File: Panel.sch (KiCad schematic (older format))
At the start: 11 parts, among them J7 Rotated_Barrel, U7 LM3406HV

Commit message: Removed the LV-Caps with the HV-Caps to remain consistent
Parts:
- C24, C26: footprint Capacitor_SMD:C_0603_1608Metric -> Capacitor_SMD:C_0805_2012Metric; Buy https://www.digikey.com/product-detail/en/murata-electronics-north-america/GCM188R71C104KA37D/490-4774-1-ND/1641693 -> https://www.digikey.com/product-detail/en/murata-electronics-north-america/GCM21BR72A104KA37L/490-4789-1-ND/1641708
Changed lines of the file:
@@
 F 0 "C29" H 1785 2220 50  0000 L CNN
 F 1 "100nF" H 1785 2070 50  0000 L CNN
-F 2 "Capacitor_SMD:C_0603_1608Metric" H 1775 2150 50  0001 C CNN
+F 2 "Capacitor_SMD:C_0805_2012Metric" H 1775 2150 50  0001 C CNN
 F 3 "" H 1775 2150 50  0001 C CNN
-F 4 "https://www.digikey.com/product-detail/en/murata-electronics-north-america/GCM188R71C104KA37D/490-4774-1-ND/1641693" H 1775 2150 60  0001 C CNN "Buy"
+F 4 "https://www.digikey.com/product-detail/en/murata-electronics-north-america/GCM21BR72A104KA37L/490-4789-1-ND/1641708" H 1775 2150 60  0001 C CNN "Buy"
 	1    1775 2150
 	1    0    0    -1
@@
 F 0 "C31" H 2985 2220 50  0000 L CNN
 F 1 "100nF" H 2985 2070 50  0000 L CNN
-F 2 "Capacitor_SMD:C_0603_1608Metric" H 2975 2150 50  0001 C CNN
+F 2 "Capacitor_SMD:C_0805_2012Metric" H 2975 2150 50  0001 C CNN
 F 3 "" H 2975 2150 50  0001 C CNN
-F 4 "https://www.digikey.com/product-detail/en/murata-electronics-north-america/GCM188R71C104KA37D/490-4774-1-ND/1641693" H 2975 2150 50  0001 C CNN "Buy"
+F 4 "https://www.digikey.com/product-detail/en/murata-electronics-north-america/GCM21BR72A104KA37L/490-4789-1-ND/1641708" H 2975 2150 50  0001 C CNN "Buy"
 	1    2975 2150
 	1    0    0    -1

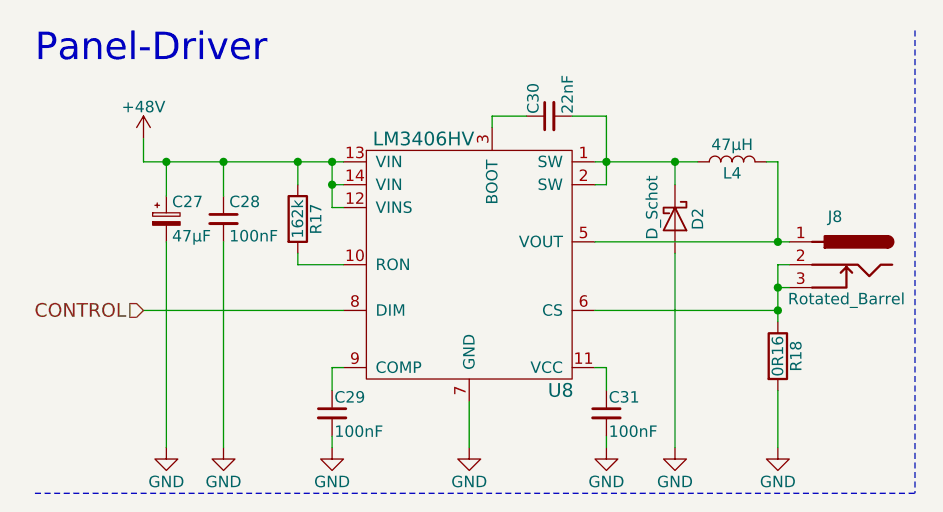
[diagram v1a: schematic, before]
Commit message: Replaced the 160mOhms-Resistor with an in-stock-one
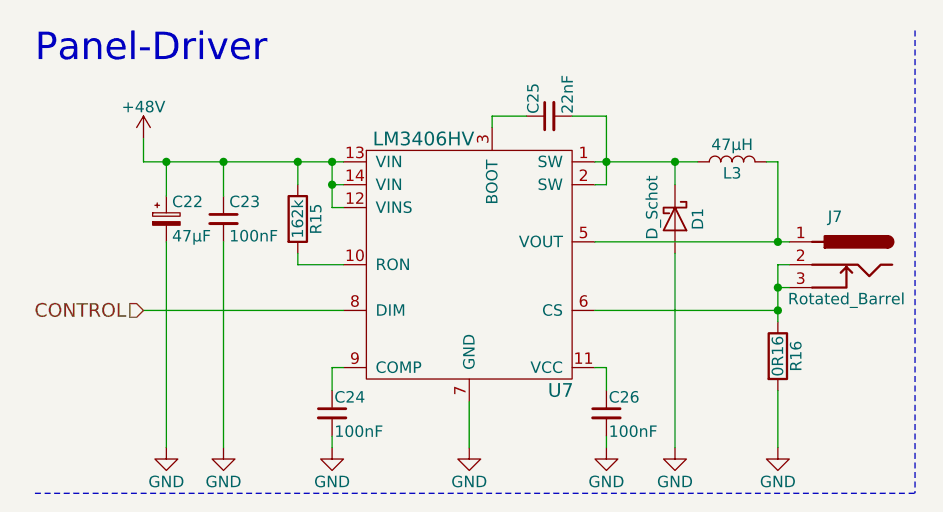
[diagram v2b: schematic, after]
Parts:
- R16: footprint Resistor_SMD:R_0805_2012Metric -> Resistor_SMD:R_1206_3216Metric; Buy https://www.digikey.com/product-detail/en/panasonic-electro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 -> https://www.digikey.com/product-detail/en/te-connectivity-p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
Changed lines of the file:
@@
 $Descr A4 11693 8268
 encoding utf-8
-Sheet 4 7
+Sheet 3 7
 Title ""
 Date "2018-02-14"
@@
 AR Path="/5A4C34AF/5A7753B7" Ref="R15"  Part="1"
 AR Path="/5A4C3F5F/5A7753B7" Ref="R17"  Part="1"
-F 0 "R17" V 1705 1300 50  0000 C CNN
+F 0 "R15" V 1705 1300 50  0000 C CNN
 F 1 "162k" V 1625 1300 50  0000 C CNN
 F 2 "Resistor_SMD:R_0603_1608Metric" V 1555 1300 50  0001 C CNN
@@
 AR Path="/5A4C34AF/5A77745B" Ref="C24"  Part="1"
 AR Path="/5A4C3F5F/5A77745B" Ref="C29"  Part="1"
-F 0 "C29" H 1785 2220 50  0000 L CNN
+F 0 "C24" H 1785 2220 50  0000 L CNN
 F 1 "100nF" H 1785 2070 50  0000 L CNN
 F 2 "Capacitor_SMD:C_0805_2012Metric" H 1775 2150 50  0001 C CNN
@@
 AR Path="/5A4C34AF/5A777BDD" Ref="#PWR063"  Part="1"
 AR Path="/5A4C3F5F/5A777BDD" Ref="#PWR071"  Part="1"
-F 0 "#PWR071" H 1775 2050 50  0001 C CNN
+F 0 "#PWR063" H 1775 2050 50  0001 C CNN
 F 1 "GND" H 1775 2150 50  0000 C CNN
 F 2 "" H 1775 2300 50  0001 C CNN
@@
 AR Path="/5A4C34AF/5A777CD4" Ref="C26"  Part="1"
 AR Path="/5A4C3F5F/5A777CD4" Ref="C31"  Part="1"
-F 0 "C31" H 2985 2220 50  0000 L CNN
+F 0 "C26" H 2985 2220 50  0000 L CNN
 F 1 "100nF" H 2985 2070 50  0000 L CNN
 F 2 "Capacitor_SMD:C_0805_2012Metric" H 2975 2150 50  0001 C CNN
@@
 AR Path="/5A4C34AF/5A777CDA" Ref="#PWR065"  Part="1"
 AR Path="/5A4C3F5F/5A777CDA" Ref="#PWR073"  Part="1"
-F 0 "#PWR073" H 2975 2050 50  0001 C CNN
+F 0 "#PWR065" H 2975 2050 50  0001 C CNN
 F 1 "GND" H 2975 2150 50  0000 C CNN
 F 2 "" H 2975 2300 50  0001 C CNN
@@
 AR Path="/5A4C34AF/5A777FA3" Ref="#PWR064"  Part="1"
 AR Path="/5A4C3F5F/5A777FA3" Ref="#PWR072"  Part="1"
-F 0 "#PWR072" H 2375 2050 50  0001 C CNN
+F 0 "#PWR064" H 2375 2050 50  0001 C CNN
 F 1 "GND" H 2375 2150 50  0000 C CNN
 F 2 "" H 2375 2300 50  0001 C CNN
@@
 AR Path="/5A4C34AF/5A77816D" Ref="C25"  Part="1"
 AR Path="/5A4C3F5F/5A77816D" Ref="C30"  Part="1"
-F 0 "C30" H 2735 920 50  0000 L CNN
+F 0 "C25" H 2735 920 50  0000 L CNN
 F 1 "22nF" H 2735 770 50  0000 L CNN
 F 2 "Capacitor_SMD:C_0603_1608Metric" H 2725 850 50  0001 C CNN
@@
 AR Path="/5A4C34AF/5A77899A" Ref="L3"  Part="1"
 AR Path="/5A4C3F5F/5A77899A" Ref="L4"  Part="1"
-F 0 "L4" V 3475 1050 50  0000 C CNN
+F 0 "L3" V 3475 1050 50  0000 C CNN
 F 1 "47μH" V 3600 1050 50  0000 C CNN
 F 2 "" H 3525 1050 50  0001 C CNN
@@
 AR Path="/5A4C34AF/5A7789F9" Ref="D1"  Part="1"
 AR Path="/5A4C3F5F/5A7789F9" Ref="D2"  Part="1"
-F 0 "D2" H 3275 1400 50  0000 C CNN
+F 0 "D1" H 3275 1400 50  0000 C CNN
 F 1 "D_Schot" H 3225 1200 50  0000 C CNN
 F 2 "Diode_SMD:D_SMA_Handsoldering" H 3275 1300 50  0001 C CNN
@@
 AR Path="/5A4C34AF/5A778B62" Ref="#PWR066"  Part="1"
 AR Path="/5A4C3F5F/5A778B62" Ref="#PWR074"  Part="1"
-F 0 "#PWR074" H 3275 2050 50  0001 C CNN
+F 0 "#PWR066" H 3275 2050 50  0001 C CNN
 F 1 "GND" H 3275 2150 50  0000 C CNN
 F 2 "" H 3275 2300 50  0001 C CNN
@@
 AR Path="/5A4C34AF/5A779AD3" Ref="J7"  Part="1"
 AR Path="/5A4C3F5F/5A779AD3" Ref="J8"  Part="1"
-F 0 "J8" H 3975 1710 50  0000 C CNN
+F 0 "J7" H 3975 1710 50  0000 C CNN
 F 1 "Rotated_Barrel" H 4025 1350 50  0000 C CNN
 F 2 "" H 4025 1440 50  0001 C CNN
@@
 AR Path="/5A4C34AF/5A77A2E1" Ref="R16"  Part="1"
 AR Path="/5A4C3F5F/5A77A2E1" Ref="R18"  Part="1"
-F 0 "R18" V 3805 1900 50  0000 C CNN
+F 0 "R16" V 3805 1900 50  0000 C CNN
 F 1 "0R16" V 3725 1900 50  0000 C CNN
-F 2 "Resistor_SMD:R_0805_2012Metric" V 3655 1900 50  0001 C CNN
+F 2 "Resistor_SMD:R_1206_3216Metric" V 3655 1900 50  0001 C CNN
 F 3 "" H 3725 1900 50  0001 C CNN
-F 4 "https://www.digikey.com/product-detail/en/panasonic-electronic-components/ERJ-6DSFR16V/P19313CT-ND/6004668" V 3725 1900 60  0001 C CNN "Buy"
+F 4 "https://www.digikey.com/product-detail/en/te-connectivity-passive-product/RLP73K2BR16FTDF/A109650CT-ND/4032416" V 3725 1900 60  0001 C CNN "Buy"
 	1    3725 1900
 	1    0    0    -1
@@
 AR Path="/5A4C34AF/5A77A9CB" Ref="#PWR067"  Part="1"
 AR Path="/5A4C3F5F/5A77A9CB" Ref="#PWR075"  Part="1"
-F 0 "#PWR075" H 3725 2050 50  0001 C CNN
+F 0 "#PWR067" H 3725 2050 50  0001 C CNN
 F 1 "GND" H 3725 2150 50  0000 C CNN
 F 2 "" H 3725 2300 50  0001 C CNN
@@
 AR Path="/5A4C34AF/5A77D43C" Ref="#PWR062"  Part="1"
 AR Path="/5A4C3F5F/5A77D43C" Ref="#PWR070"  Part="1"
-F 0 "#PWR070" H 1300 2050 50  0001 C CNN
+F 0 "#PWR062" H 1300 2050 50  0001 C CNN
 F 1 "GND" H 1300 2150 50  0000 C CNN
 F 2 "" H 1300 2300 50  0001 C CNN
@@
 AR Path="/5A4C34AF/5A77E620" Ref="U7"  Part="1"
 AR Path="/5A4C3F5F/5A77E620" Ref="U8"  Part="1"
-F 0 "U8" H 2775 950 60  0000 C CNN
+F 0 "U7" H 2775 950 60  0000 C CNN
 F 1 "LM3406HV" H 2175 2050 60  0000 C CNN
 F 2 "Package_SO:TSSOP-14_4.4x5mm_P0.65mm" H 2375 2100 60  0001 C CNN
@@
 AR Path="/5A4C34AF/5A84C99A" Ref="#PWR060"  Part="1"
 AR Path="/5A4C3F5F/5A84C99A" Ref="#PWR068"  Part="1"
-F 0 "#PWR068" H 950 800 50  0001 C CNN
+F 0 "#PWR060" H 950 800 50  0001 C CNN
 F 1 "+48V" H 950 1090 50  0000 C CNN
 F 2 "" H 950 950 50  0001 C CNN
@@
 AR Path="/5A4C34AF/5ABA3DDA" Ref="C22"  Part="1"
 AR Path="/5A4C3F5F/5ABA3DDA" Ref="C27"  Part="1"
-F 0 "C27" H 1075 1375 50  0000 L CNN
+F 0 "C22" H 1075 1375 50  0000 L CNN
 F 1 "47μF" H 1075 1225 50  0000 L CNN
 F 2 "" H 1050 1300 50  0001 C CNN
@@
 AR Path="/5A4C34AF/5ABA5E6C" Ref="C23"  Part="1"
 AR Path="/5A4C3F5F/5ABA5E6C" Ref="C28"  Part="1"
-F 0 "C28" H 1325 1375 50  0000 L CNN
+F 0 "C23" H 1325 1375 50  0000 L CNN
 F 1 "100nF" H 1325 1225 50  0000 L CNN
 F 2 "Capacitor_SMD:C_0805_2012Metric" H 1300 1300 50  0001 C CNN
@@
 AR Path="/5A4C34AF/5ABA815F" Ref="#PWR061"  Part="1"
 AR Path="/5A4C3F5F/5ABA815F" Ref="#PWR069"  Part="1"
-F 0 "#PWR069" H 1050 2050 50  0001 C CNN
+F 0 "#PWR061" H 1050 2050 50  0001 C CNN
 F 1 "GND" H 1050 2150 50  0000 C CNN
 F 2 "" H 1050 2300 50  0001 C CNN

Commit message: Replaced the LM3406 with an in-stock-one
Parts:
- U7: Buy https://www.digikey.com/product-detail/en/texas-instruments/LM3406HVMHX-NOPB/LM3406HVMHX-NOPBCT-ND/3526958 -> https://www.digikey.com/product-detail/en/texas-instruments/LM3406HVQMHXQ1/296-38110-1-ND/4967315
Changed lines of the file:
@@
 F 2 "Package_SO:TSSOP-14_4.4x5mm_P0.65mm" H 2375 2100 60  0001 C CNN
 F 3 "http://www.ti.com/lit/ds/symlink/lm3406.pdf" H 2375 2100 60  0001 C CNN
-F 4 "https://www.digikey.com/product-detail/en/texas-instruments/LM3406HVMHX-NOPB/LM3406HVMHX-NOPBCT-ND/3526958" H 2375 1500 60  0001 C CNN "Buy"
+F 4 "https://www.digikey.com/product-detail/en/texas-instruments/LM3406HVQMHXQ1/296-38110-1-ND/4967315" H 2375 1500 60  0001 C CNN "Buy"
 	1    2375 1500
 	1    0    0    -1

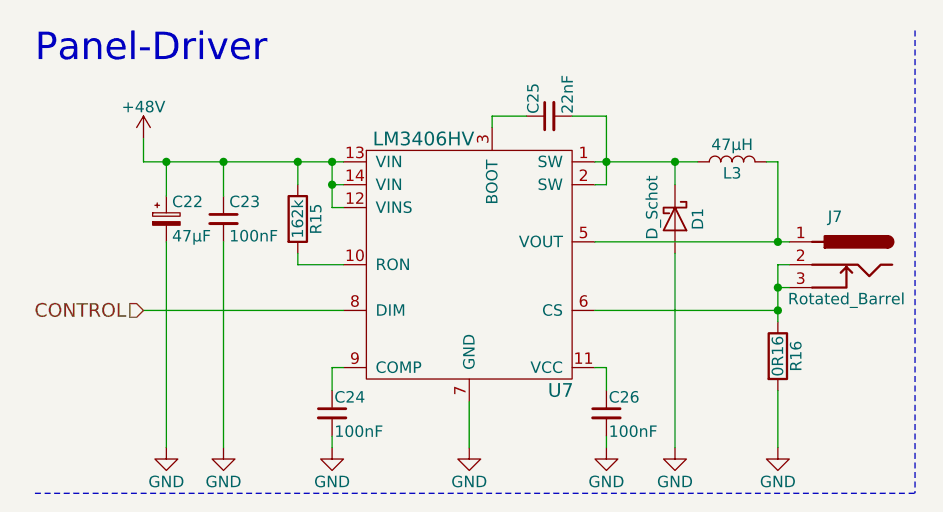
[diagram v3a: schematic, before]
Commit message: Purged the LM3406-Footprintfield
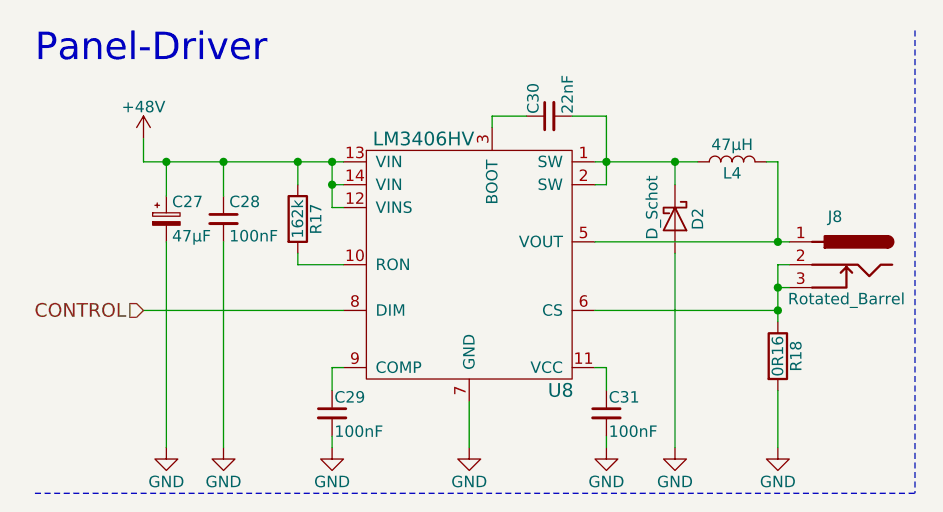
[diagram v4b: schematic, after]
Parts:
- U7: footprint Package_SO:TSSOP-14_4.4x5mm_P0.65mm -> (none)
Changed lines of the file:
@@
 $Descr A4 11693 8268
 encoding utf-8
-Sheet 3 7
+Sheet 4 7
 Title ""
 Date "2018-02-14"
@@
 AR Path="/5A4C34AF/5A7753B7" Ref="R15"  Part="1"
 AR Path="/5A4C3F5F/5A7753B7" Ref="R17"  Part="1"
-F 0 "R15" V 1705 1300 50  0000 C CNN
+F 0 "R17" V 1705 1300 50  0000 C CNN
 F 1 "162k" V 1625 1300 50  0000 C CNN
 F 2 "Resistor_SMD:R_0603_1608Metric" V 1555 1300 50  0001 C CNN
@@
 AR Path="/5A4C34AF/5A77745B" Ref="C24"  Part="1"
 AR Path="/5A4C3F5F/5A77745B" Ref="C29"  Part="1"
-F 0 "C24" H 1785 2220 50  0000 L CNN
+F 0 "C29" H 1785 2220 50  0000 L CNN
 F 1 "100nF" H 1785 2070 50  0000 L CNN
 F 2 "Capacitor_SMD:C_0805_2012Metric" H 1775 2150 50  0001 C CNN
@@
 AR Path="/5A4C34AF/5A777BDD" Ref="#PWR063"  Part="1"
 AR Path="/5A4C3F5F/5A777BDD" Ref="#PWR071"  Part="1"
-F 0 "#PWR063" H 1775 2050 50  0001 C CNN
+F 0 "#PWR071" H 1775 2050 50  0001 C CNN
 F 1 "GND" H 1775 2150 50  0000 C CNN
 F 2 "" H 1775 2300 50  0001 C CNN
@@
 AR Path="/5A4C34AF/5A777CD4" Ref="C26"  Part="1"
 AR Path="/5A4C3F5F/5A777CD4" Ref="C31"  Part="1"
-F 0 "C26" H 2985 2220 50  0000 L CNN
+F 0 "C31" H 2985 2220 50  0000 L CNN
 F 1 "100nF" H 2985 2070 50  0000 L CNN
 F 2 "Capacitor_SMD:C_0805_2012Metric" H 2975 2150 50  0001 C CNN
@@
 AR Path="/5A4C34AF/5A777CDA" Ref="#PWR065"  Part="1"
 AR Path="/5A4C3F5F/5A777CDA" Ref="#PWR073"  Part="1"
-F 0 "#PWR065" H 2975 2050 50  0001 C CNN
+F 0 "#PWR073" H 2975 2050 50  0001 C CNN
 F 1 "GND" H 2975 2150 50  0000 C CNN
 F 2 "" H 2975 2300 50  0001 C CNN
@@
 AR Path="/5A4C34AF/5A777FA3" Ref="#PWR064"  Part="1"
 AR Path="/5A4C3F5F/5A777FA3" Ref="#PWR072"  Part="1"
-F 0 "#PWR064" H 2375 2050 50  0001 C CNN
+F 0 "#PWR072" H 2375 2050 50  0001 C CNN
 F 1 "GND" H 2375 2150 50  0000 C CNN
 F 2 "" H 2375 2300 50  0001 C CNN
@@
 AR Path="/5A4C34AF/5A77816D" Ref="C25"  Part="1"
 AR Path="/5A4C3F5F/5A77816D" Ref="C30"  Part="1"
-F 0 "C25" H 2735 920 50  0000 L CNN
+F 0 "C30" H 2735 920 50  0000 L CNN
 F 1 "22nF" H 2735 770 50  0000 L CNN
 F 2 "Capacitor_SMD:C_0603_1608Metric" H 2725 850 50  0001 C CNN
@@
 AR Path="/5A4C34AF/5A77899A" Ref="L3"  Part="1"
 AR Path="/5A4C3F5F/5A77899A" Ref="L4"  Part="1"
-F 0 "L3" V 3475 1050 50  0000 C CNN
+F 0 "L4" V 3475 1050 50  0000 C CNN
 F 1 "47μH" V 3600 1050 50  0000 C CNN
 F 2 "" H 3525 1050 50  0001 C CNN
@@
 AR Path="/5A4C34AF/5A7789F9" Ref="D1"  Part="1"
 AR Path="/5A4C3F5F/5A7789F9" Ref="D2"  Part="1"
-F 0 "D1" H 3275 1400 50  0000 C CNN
+F 0 "D2" H 3275 1400 50  0000 C CNN
 F 1 "D_Schot" H 3225 1200 50  0000 C CNN
 F 2 "Diode_SMD:D_SMA_Handsoldering" H 3275 1300 50  0001 C CNN
@@
 AR Path="/5A4C34AF/5A778B62" Ref="#PWR066"  Part="1"
 AR Path="/5A4C3F5F/5A778B62" Ref="#PWR074"  Part="1"
-F 0 "#PWR066" H 3275 2050 50  0001 C CNN
+F 0 "#PWR074" H 3275 2050 50  0001 C CNN
 F 1 "GND" H 3275 2150 50  0000 C CNN
 F 2 "" H 3275 2300 50  0001 C CNN
@@
 AR Path="/5A4C34AF/5A779AD3" Ref="J7"  Part="1"
 AR Path="/5A4C3F5F/5A779AD3" Ref="J8"  Part="1"
-F 0 "J7" H 3975 1710 50  0000 C CNN
+F 0 "J8" H 3975 1710 50  0000 C CNN
 F 1 "Rotated_Barrel" H 4025 1350 50  0000 C CNN
 F 2 "" H 4025 1440 50  0001 C CNN
@@
 AR Path="/5A4C34AF/5A77A2E1" Ref="R16"  Part="1"
 AR Path="/5A4C3F5F/5A77A2E1" Ref="R18"  Part="1"
-F 0 "R16" V 3805 1900 50  0000 C CNN
+F 0 "R18" V 3805 1900 50  0000 C CNN
 F 1 "0R16" V 3725 1900 50  0000 C CNN
 F 2 "Resistor_SMD:R_1206_3216Metric" V 3655 1900 50  0001 C CNN
@@
 AR Path="/5A4C34AF/5A77A9CB" Ref="#PWR067"  Part="1"
 AR Path="/5A4C3F5F/5A77A9CB" Ref="#PWR075"  Part="1"
-F 0 "#PWR067" H 3725 2050 50  0001 C CNN
+F 0 "#PWR075" H 3725 2050 50  0001 C CNN
 F 1 "GND" H 3725 2150 50  0000 C CNN
 F 2 "" H 3725 2300 50  0001 C CNN
@@
 AR Path="/5A4C34AF/5A77D43C" Ref="#PWR062"  Part="1"
 AR Path="/5A4C3F5F/5A77D43C" Ref="#PWR070"  Part="1"
-F 0 "#PWR062" H 1300 2050 50  0001 C CNN
+F 0 "#PWR070" H 1300 2050 50  0001 C CNN
 F 1 "GND" H 1300 2150 50  0000 C CNN
 F 2 "" H 1300 2300 50  0001 C CNN
@@
 AR Path="/5A4C34AF/5A77E620" Ref="U7"  Part="1"
 AR Path="/5A4C3F5F/5A77E620" Ref="U8"  Part="1"
-F 0 "U7" H 2775 950 60  0000 C CNN
+F 0 "U8" H 2775 950 60  0000 C CNN
 F 1 "LM3406HV" H 2175 2050 60  0000 C CNN
-F 2 "Package_SO:TSSOP-14_4.4x5mm_P0.65mm" H 2375 2100 60  0001 C CNN
+F 2 "" H 2375 2100 60  0001 C CNN
 F 3 "http://www.ti.com/lit/ds/symlink/lm3406.pdf" H 2375 2100 60  0001 C CNN
 F 4 "https://www.digikey.com/product-detail/en/texas-instruments/LM3406HVQMHXQ1/296-38110-1-ND/4967315" H 2375 1500 60  0001 C CNN "Buy"
@@
 AR Path="/5A4C34AF/5A84C99A" Ref="#PWR060"  Part="1"
 AR Path="/5A4C3F5F/5A84C99A" Ref="#PWR068"  Part="1"
-F 0 "#PWR060" H 950 800 50  0001 C CNN
+F 0 "#PWR068" H 950 800 50  0001 C CNN
 F 1 "+48V" H 950 1090 50  0000 C CNN
 F 2 "" H 950 950 50  0001 C CNN
@@
 AR Path="/5A4C34AF/5ABA3DDA" Ref="C22"  Part="1"
 AR Path="/5A4C3F5F/5ABA3DDA" Ref="C27"  Part="1"
-F 0 "C22" H 1075 1375 50  0000 L CNN
+F 0 "C27" H 1075 1375 50  0000 L CNN
 F 1 "47μF" H 1075 1225 50  0000 L CNN
 F 2 "" H 1050 1300 50  0001 C CNN
@@
 AR Path="/5A4C34AF/5ABA5E6C" Ref="C23"  Part="1"
 AR Path="/5A4C3F5F/5ABA5E6C" Ref="C28"  Part="1"
-F 0 "C23" H 1325 1375 50  0000 L CNN
+F 0 "C28" H 1325 1375 50  0000 L CNN
 F 1 "100nF" H 1325 1225 50  0000 L CNN
 F 2 "Capacitor_SMD:C_0805_2012Metric" H 1300 1300 50  0001 C CNN
@@
 AR Path="/5A4C34AF/5ABA815F" Ref="#PWR061"  Part="1"
 AR Path="/5A4C3F5F/5ABA815F" Ref="#PWR069"  Part="1"
-F 0 "#PWR061" H 1050 2050 50  0001 C CNN
+F 0 "#PWR069" H 1050 2050 50  0001 C CNN
 F 1 "GND" H 1050 2150 50  0000 C CNN
 F 2 "" H 1050 2300 50  0001 C CNN
